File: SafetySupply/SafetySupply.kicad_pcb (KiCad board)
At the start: 2 copper layers, 30 x 60 mm, 51 parts, among them J1 Screw_Terminal_01x02, J2 Conn_01x01, J3 Screw_Terminal_01x02, J4 Conn_01x01, J5 Screw_Terminal_01x02, J6 Conn_01x01, J7 Conn_01x01, J8 Conn_01x01, J9 Conn_01x01, K1 FRM18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

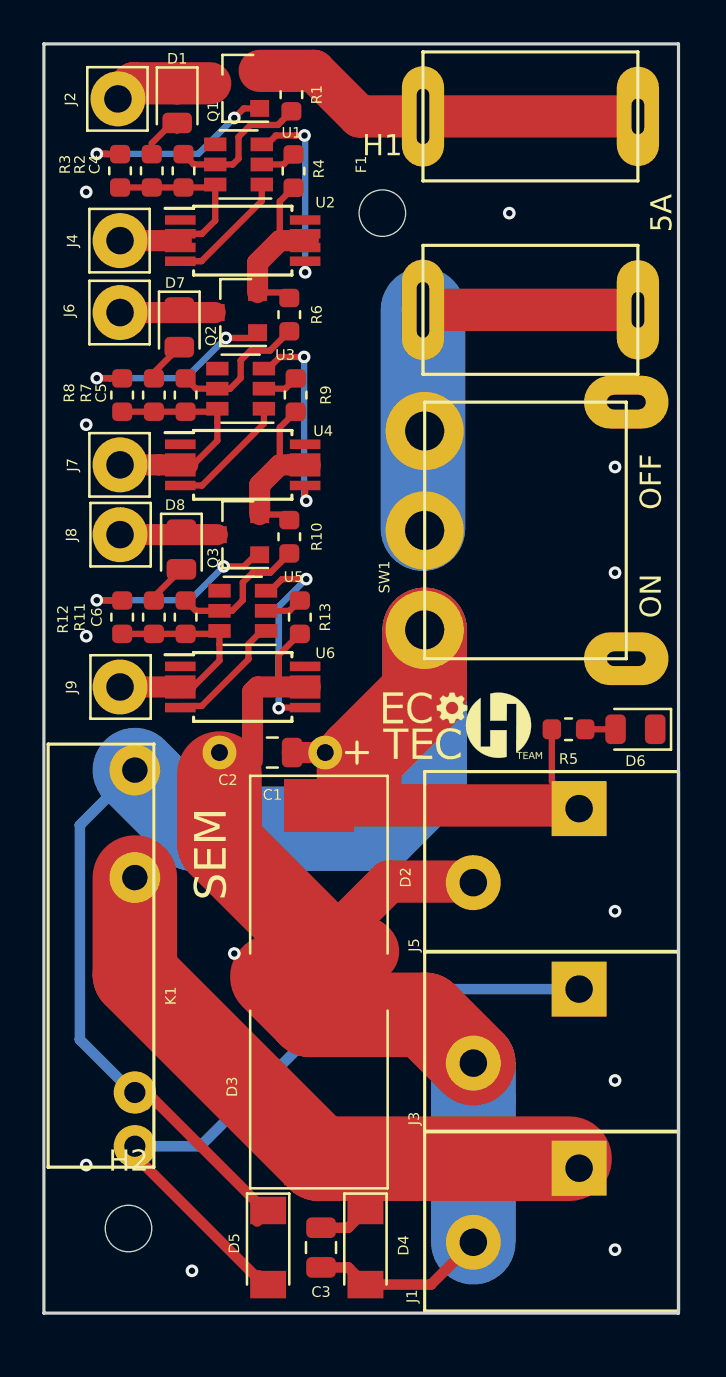
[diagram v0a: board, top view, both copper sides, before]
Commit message: Added 3D models to the library
Squashed commit of the following:

commit 8070c09fc3d8f70a7cb84d0f12b6782c2c87c14c
Author: Paweł <mackipawel@gmail.com>
Date:   Mon May 6 20:26:56 2019 +0200

    Added SystemSupply 3d models.

commit 94ef8708632c7bc91211bc6ded4e0c8fb9ccef4a
Author: Paweł <mackipawel@gmail.com>
Date:   Mon May 6 01:08:52 2019 +0200

    Added 3D models to SystemSupply.

commit eb394d70be979be958e4acab21accb1817e8e0e5
Author: Paweł <mackipawel@gmail.com>
Date:   Mon May 6 00:55:39 2019 +0200

    Added 3D model to MotorController.

commit fd89e01e0ef36f85afad3e8686d3deffdf36454d
Author: Paweł <mackipawel@gmail.com>
Date:   Mon May 6 00:40:56 2019 +0200

    Added 3D models in MotorDriver.

commit 899d106fa8d45578189a4955328047d8f9558beb
Author: Paweł <mackipawel@gmail.com>
Date:   Mon May 6 00:09:40 2019 +0200

    Added 3D models to SafetySupply.

commit 06c807994bb47431d2802a96796741a0e8fb9ae5
Author: Paweł <mackipawel@gmail.com>
Date:   Sun May 5 23:17:48 2019 +0200

    Added 3D models to SafetySystem.
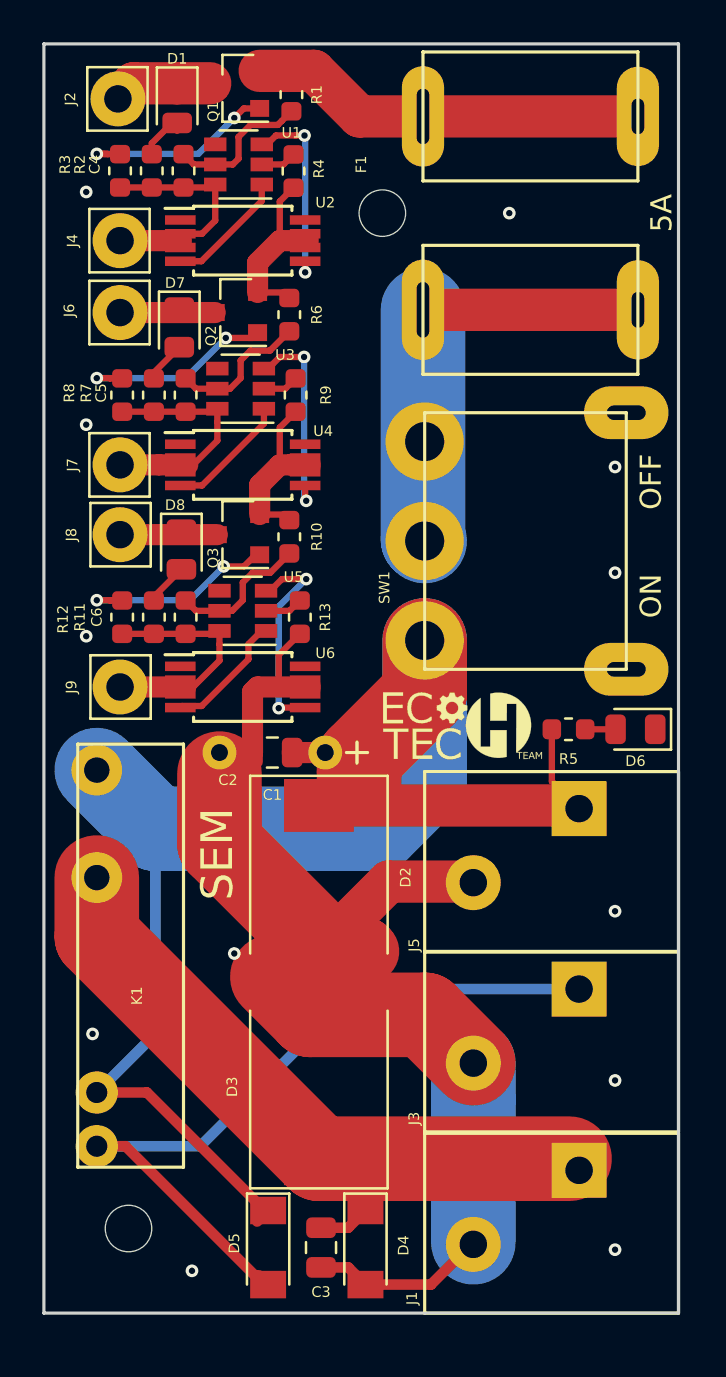
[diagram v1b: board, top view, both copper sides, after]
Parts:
- moved K1 1.60 mm to (136.6, 104.1)
- moved SW1 0.50 mm to (158.0, 84.5)
- moved J1 0.10 mm to (165.0, 112.5)
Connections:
- SW1 pad 0: (no net) -> GND
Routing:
- net Net-(D5-Pad2): track 34.0 -> 37.3 mm
- net +12V: track 76.7 -> 74.8 mm
- net Net-(C3-Pad1): track 34.2 -> 35.0 mm
- net Net-(F1-Pad1): track 20.7 -> 21.3 mm

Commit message: Adding gerbers
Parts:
- renumbered G1 to ?

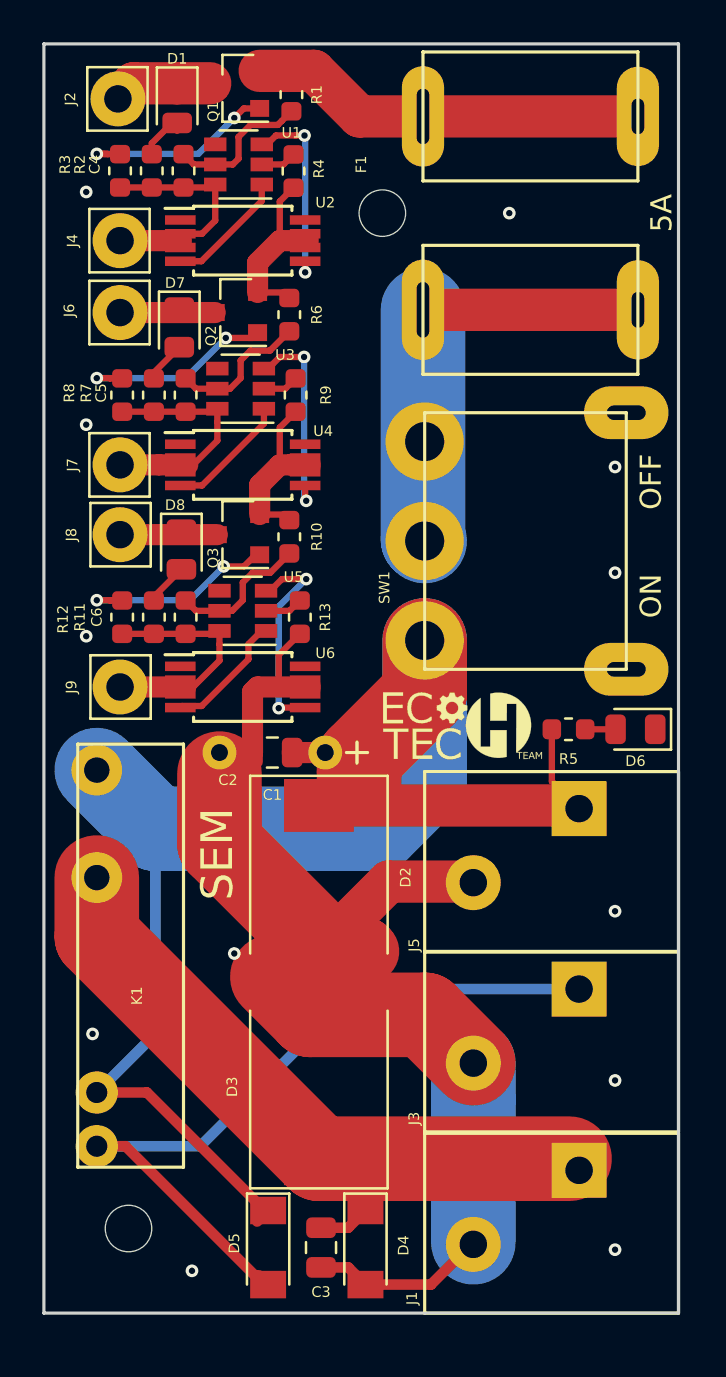
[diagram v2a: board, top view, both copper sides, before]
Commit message: Changed all via diameters to 0.7. Added project and version label on silk screen. Added more grounding vias.
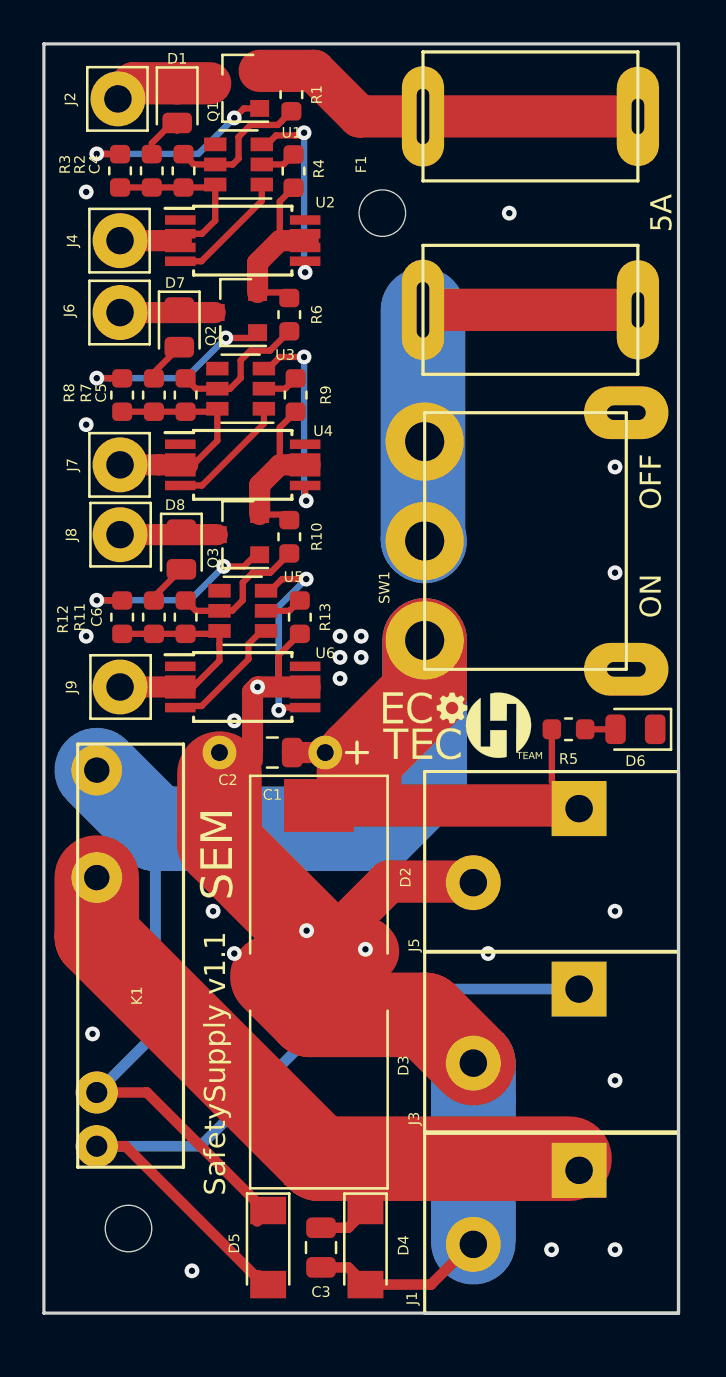
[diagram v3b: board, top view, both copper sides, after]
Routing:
- net GND: track 61.4 -> 63.4 mm, vias 12 -> 24
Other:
- net class Default: via_dia 0.6 -> 0.7
- rule via_min_size: 0.4 -> 0.7
- board text added: "SafetySupply v1.1"

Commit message: Changed 1.1 to 1.0 versions.
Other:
- board text added: "SafetySupply v1.0"
- board text removed: "SafetySupply v1.1"
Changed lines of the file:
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@@
     )
   )
-  (gr_text "SafetySupply v1.1" (at 143.1 109.2 90) (layer F.SilkS)
+  (gr_text "SafetySupply v1.0" (at 143.1 109.2 90) (layer F.SilkS)
     (effects (font (size 1 1) (thickness 0.2)))
   )

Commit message: Added version date on silk screen and changed signal tracks width to 0,2.
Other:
- board text added: "SafetySupply v1.0 12.05.2019"
- board text removed: "SafetySupply v1.0"
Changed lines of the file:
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@@
     (user_trace_width 4)
     (trace_clearance 0.2)
-    (zone_clearance 0.25)
+    (zone_clearance 0.2)
     (zone_45_only no)
     (trace_min 0.2)
@@
   (module Footprints:Fuse_Blade_90 (layer F.Cu)
     (at 158 69 90)
-    (fp_text reference F1 (at 2.3 -8 270) (layer F.SilkS)
+    (fp_text reference F1 (at -3 -8 270) (layer F.SilkS)
       (effects (font (size 0.5 0.5) (thickness 0.1)))
     )
@@
     )
   )
-  (gr_text "SafetySupply v1.0" (at 143.1 109.2 90) (layer F.SilkS)
+  (gr_text "SafetySupply v1.0 12.05.2019" (at 143.1 108.4 90) (layer F.SilkS)
     (effects (font (size 1 1) (thickness 0.2)))
   )
-  (gr_text SEM (at 143.2 99.3 90) (layer F.SilkS)
-    (effects (font (size 1.5 1.5) (thickness 0.2)))
+  (gr_text SEM (at 150 65 90) (layer F.SilkS)
+    (effects (font (size 2 2) (thickness 0.3)))
   )
   (gr_text OFF (at 163.7 81.7 90) (layer F.SilkS)
@@
   (segment (start 152.92 73.572) (end 152.92 84.42) (width 4) (layer B.Cu) (net 39))
   (zone (net 7) (net_name GND) (layer F.Cu) (hatch edge 0.508)
-    (connect_pads (clearance 0.25))
-    (min_thickness 0.25)
-    (fill yes (arc_segments 16) (thermal_gap 0.3) (thermal_bridge_width 0.4))
+    (connect_pads (clearance 0.2))
+    (min_thickness 0.2)
+    (fill yes (arc_segments 16) (thermal_gap 0.2) (thermal_bridge_width 0.4))
     (polygon
       (pts
@@
   )
   (zone (net 7) (net_name GND) (layer B.Cu) (hatch edge 0.508)
-    (connect_pads (clearance 0.25))
-    (min_thickness 0.25)
-    (fill yes (arc_segments 16) (thermal_gap 0.3) (thermal_bridge_width 0.4))
+    (connect_pads (clearance 0.2))
+    (min_thickness 0.2)
+    (fill yes (arc_segments 16) (thermal_gap 0.2) (thermal_bridge_width 0.4))
     (polygon
       (pts
